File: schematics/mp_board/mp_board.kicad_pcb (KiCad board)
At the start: 4 copper layers, 49 parts, among them J1 i2c_1, J10 swd, J11 stm_boot, J17 rst_mcu, J2 i2c_2, J3 pins_b, J4 power_a, J6 MY_USB_B, J7 power_b, J8 pins_a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

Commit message: Placing components...
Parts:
- moved C5 104.2 mm to (169.5, 92.0), turned to -90 degrees
- moved C1 101.2 mm to (162.7, 92.2), turned to 90 degrees
- moved C28 100.6 mm to (151.7, 113.5), turned to 180 degrees
- moved J6 100.5 mm to (169.0, 102.8)
- moved J17 95.4 mm to (150.0, 35.0)
- moved R4 95.1 mm to (162.8, 103.8)
- moved C24 94.9 mm to (153.0, 111.8)
- moved C29 93.0 mm to (155.2, 98.5), turned to 90 degrees
- moved R3 92.0 mm to (158.7, 102.8), turned to 180 degrees
- moved C31 89.1 mm to (143.0, 113.5), turned to -90 degrees
- moved C27 87.7 mm to (153.5, 97.5), turned to 90 degrees
- moved C23 79.4 mm to (136.2, 106.5), turned to 180 degrees
- moved C30 78.0 mm to (140.0, 97.0), turned to 180 degrees
- moved U10 73.7 mm to (146.3, 104.2)
- moved J11 73.4 mm to (128.5, 50.0)
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
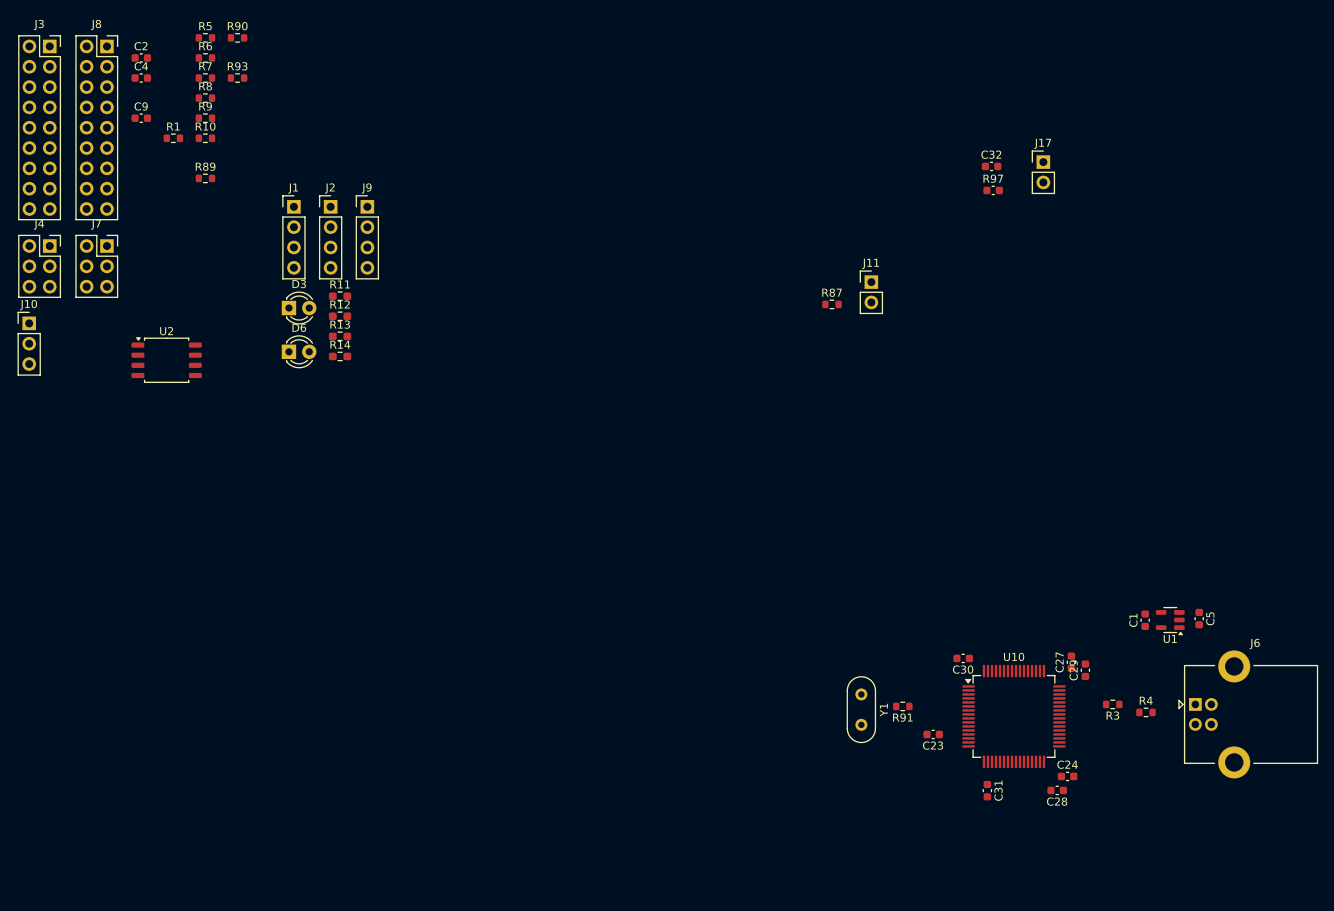
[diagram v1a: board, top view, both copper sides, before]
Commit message: Made tripple sockets. Mid pins are all ground for shielding.
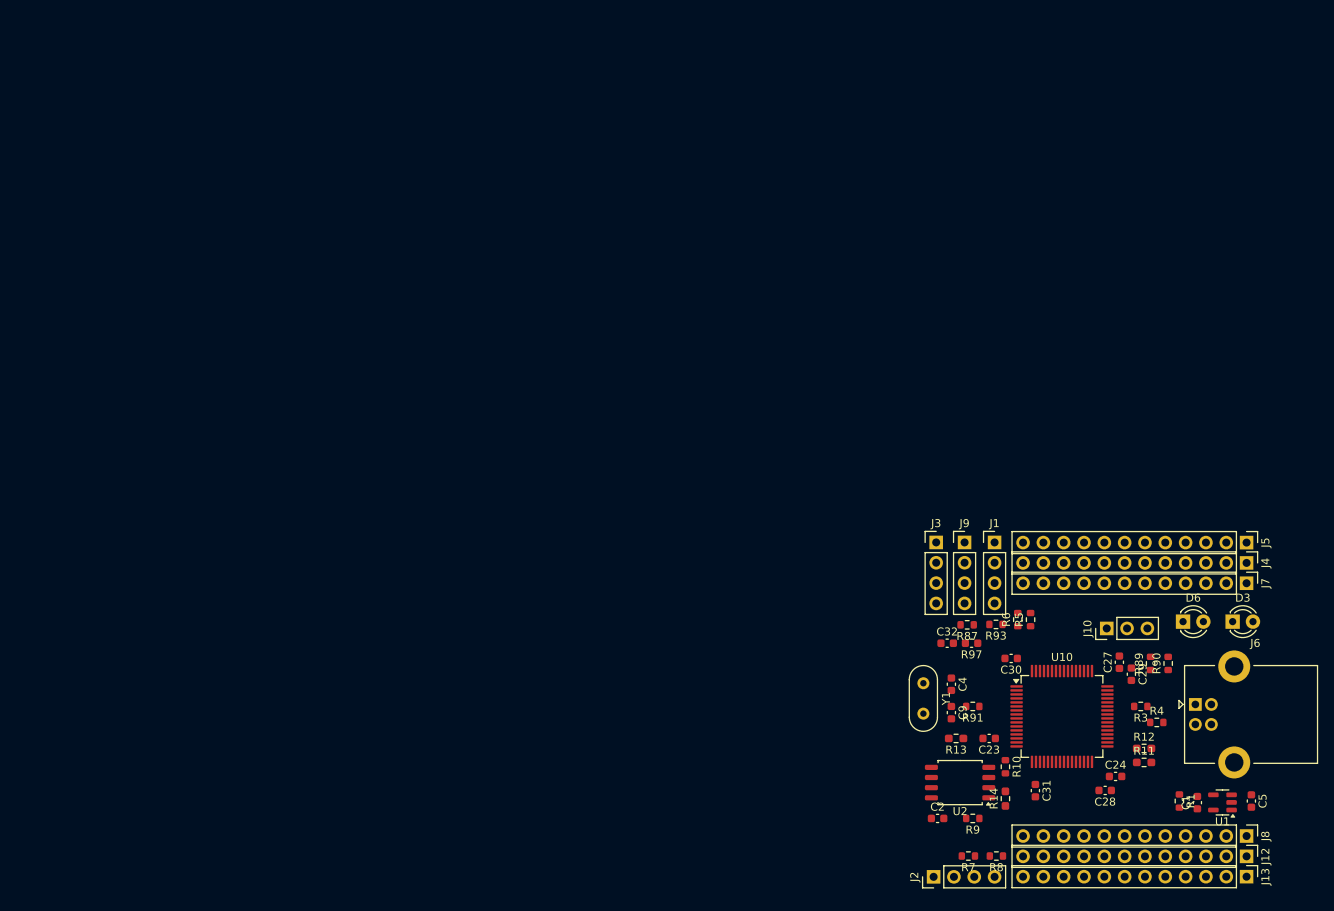
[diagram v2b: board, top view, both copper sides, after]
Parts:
- removed J11: stm_boot, Connector_PinHeader_2.54mm:PinHeader_1x02_P2.54mm_Vertical
- removed J17: rst_mcu, Connector_PinHeader_2.54mm:PinHeader_1x02_P2.54mm_Vertical
- added J12: pins_e, Connector_PinHeader_2.54mm:PinHeader_1x12_P2.54mm_Vertical, F.Cu at (175.4, 121.7)
- added J13: pins_f, Connector_PinHeader_2.54mm:PinHeader_1x12_P2.54mm_Vertical, F.Cu at (175.4, 124.3)
- added J5: pins_a, Connector_PinHeader_2.54mm:PinHeader_1x12_P2.54mm_Vertical, F.Cu at (175.4, 82.5)
- J3: value pins_b -> boot_rst; footprint Connector_PinSocket_2.54mm:PinSocket_2x09_P2.54mm_Vertical -> Connector_PinHeader_2.54mm:PinHeader_1x04_P2.54mm_Vertical
- J4: value power_a -> pins_b; footprint Connector_PinSocket_2.54mm:PinSocket_2x03_P2.54mm_Vertical -> Connector_PinHeader_2.54mm:PinHeader_1x12_P2.54mm_Vertical
- J7: value power_b -> pins_c; footprint Connector_PinSocket_2.54mm:PinSocket_2x03_P2.54mm_Vertical -> Connector_PinHeader_2.54mm:PinHeader_1x12_P2.54mm_Vertical
- J8: value pins_a -> pins_d; footprint Connector_PinSocket_2.54mm:PinSocket_2x09_P2.54mm_Vertical -> Connector_PinHeader_2.54mm:PinHeader_1x12_P2.54mm_Vertical
- moved J8 173.3 mm to (175.4, 119.2), turned to -90 degrees
- moved J4 154.8 mm to (175.4, 85.1), turned to -90 degrees
- moved R1 150.6 mm to (167.0, 114.8), turned to -90 degrees
- moved J7 148.6 mm to (175.4, 87.6), turned to -90 degrees
- moved R90 140.2 mm to (165.6, 97.6), turned to 90 degrees
- moved J10 140.0 mm to (157.9, 93.2), turned to 90 degrees
- moved C2 137.6 mm to (136.8, 117.0)
- moved R8 136.9 mm to (144.1, 121.7), turned to 180 degrees
- moved R7 136.2 mm to (140.6, 121.7), turned to 180 degrees
- moved R89 132.8 mm to (163.4, 97.6), turned to 90 degrees
- moved R9 129.9 mm to (141.2, 117.0), turned to 180 degrees
- moved R10 127.2 mm to (145.3, 110.5), turned to -90 degrees
- moved J3 127.0 mm to (136.6, 82.5)
- moved C4 126.5 mm to (138.5, 100.2), turned to -90 degrees
- moved R5 126.2 mm to (148.4, 92.2), turned to 90 degrees
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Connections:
- J3 pad 1: /pb14 -> /rst_mcu
- J3 pad 2: /pb15 -> GND
- J3 pad 3: /led-0 -> /boot0
- J3 pad 4: /pc0 -> VDD
- J4 pad 1: VDD -> GND
- J4 pad 3: /Vbus -> GND
- J4 pad 4: /Vbus -> GND
- J4 pad 6: VDD -> GND
- J7 pad 1: VDD -> /Vbus
- J7 pad 3: /Vbus -> VDD
- J7 pad 4: /Vbus -> /pa8
- J7 pad 5: GND -> /pb0
- J7 pad 6: VDD -> /pb1
- J8 pad 1: /pa0 -> /Vbus
- J8 pad 10: GND -> /pc5
- J8 pad 11: /pb8 -> /pc6
- J8 pad 12: /pb9 -> /pc15
- J8 pad 2: /pa1 -> GND
- J8 pad 3: /pa2 -> VDD
- J8 pad 4: /pa3 -> /pb14
- J8 pad 5: /pa4 -> /pb15
- J8 pad 6: /pa5 -> /led-0
- J8 pad 7: /pa6 -> /pc0
- J8 pad 8: /pa7 -> /pc1
- J8 pad 9: /pc14 -> /pc4

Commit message: a
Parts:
- moved R1 4.63 mm to (162.4, 114.3)
- moved R11 2.28 mm to (160.3, 110.1)
- moved R4 2.02 mm to (164.4, 103.0), turned to 180 degrees
- moved R3 1.98 mm to (163.5, 101.5)
- moved R12 0.79 mm to (161.8, 108.4)
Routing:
- net GND: track 0.00 -> 266.4 mm, vias 0 -> 21
- net /Vbus: track 0.00 -> 81.6 mm, vias 0 -> 4
- net VDD: track 0.00 -> 44.8 mm, vias 0 -> 7
- net /uart1-rx: track 0.00 -> 30.6 mm, vias 0 -> 2
- net /uart1-tx: track 0.00 -> 26.4 mm, vias 0 -> 1
- net /boot0: track 0.00 -> 21.4 mm
- net /spi2_miso: track 0.00 -> 21.1 mm
- net /rst_mcu: track 0.00 -> 13.8 mm
- net /boot1: track 0.00 -> 12.8 mm
- net /clk-in: track 0.00 -> 12.6 mm
- net /swd_io: track 0.00 -> 11.8 mm
- net /i2c1_sck: track 0.00 -> 10.7 mm
- net Net-(D3-K): track 0.00 -> 9.88 mm
- net Net-(J6-D+): track 0.00 -> 8.25 mm
- net /spi2_mosi: track 0.00 -> 7.27 mm
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
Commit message: Placing footprints, wiring.
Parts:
- moved C5 0.61 mm to (175.5, 115.2), turned to 90 degrees
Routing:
- net /i2c2_sck: track 0.00 -> 31.1 mm, vias 0 -> 2
- net /i2c2_sda: track 0.00 -> 28.1 mm, vias 0 -> 2
- net /rst_mcu: track 13.8 -> 33.8 mm, vias 0 -> 2
- net VDD: track 44.8 -> 49.5 mm, vias 7 -> 12
- net GND: track 266.4 -> 262.2 mm
- net /Vbus: track 81.6 -> 79.0 mm

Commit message: Wiring.
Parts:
- moved C5 0.27 mm to (175.5, 114.9), turned to -90 degrees
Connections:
- J13 pad 10: /pc13 -> /pa5
- J13 pad 11: /pd2 -> /pa3
- J13 pad 4: /pc7 -> /pb15
- J13 pad 5: /pc8 -> /pb0
- J13 pad 6: /pc9 -> /pa1
- J13 pad 8: /pc11 -> /pa2
- J13 pad 9: /pc12 -> /pa4
- J5 pad 10: /pa6 -> /pc13
- J5 pad 11: /pa7 -> /pc15
- J5 pad 12: /pc14 -> /pc0
- J5 pad 4: /pa0 -> /pc7
- J5 pad 5: /pa1 -> /pc9
- J5 pad 6: /pa2 -> /pc11
- J5 pad 7: /pa3 -> /pd2
- J5 pad 8: /pa4 -> /pb4
- J5 pad 9: /pa5 -> /pb8
- J7 pad 11: /pb8 -> /pc14
- J7 pad 4: /pa8 -> /pc6
- J7 pad 5: /pb0 -> /pc8
- J7 pad 6: /pb1 -> /pa8
- J7 pad 7: /pb3 -> /pc12
- J7 pad 8: /pb4 -> /pb3
- J8 pad 11: /pc6 -> /pb1
- J8 pad 12: /pc15 -> /pa6
- J8 pad 5: /pb15 -> /pa0
- J8 pad 7: /pc0 -> /pa7
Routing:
- net VDD: track 49.5 -> 273.1 mm, vias 12 -> 16
- net /pc7: track 0.00 -> 32.7 mm, vias 0 -> 1
- net /pc9: track 0.00 -> 31.4 mm, vias 0 -> 1
- net /flash_sck: track 1.26 -> 32.5 mm, vias 1 -> 2
- net /pb15: track 0.00 -> 30.7 mm, vias 0 -> 1
- net /pc0: track 0.00 -> 27.6 mm, vias 0 -> 1
- net /flash_cs: track 1.21 -> 27.0 mm, vias 1 -> 2
- net /pc6: track 0.00 -> 25.7 mm, vias 0 -> 1
- net /pc15: track 0.00 -> 24.9 mm, vias 0 -> 1
- net /pa8: track 0.00 -> 24.5 mm, vias 0 -> 1
- net /pc13: track 0.00 -> 24.0 mm, vias 0 -> 1
- net /pb8: track 0.00 -> 22.2 mm, vias 0 -> 1
- net /pc8: track 0.00 -> 22.0 mm, vias 0 -> 1
- net /pc14: track 0.00 -> 21.2 mm, vias 0 -> 1
- net /pc11: track 0.00 -> 20.3 mm
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
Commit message: Wiring.
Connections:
- J13 pad 10: /pa5 -> /pa3
- J13 pad 11: /pa3 -> /pa1
- J13 pad 4: /pb15 -> /pc6
- J13 pad 5: /pb0 -> /pb14
- J13 pad 6: /pa1 -> /pb1
- J13 pad 7: /led-1 -> /pc5
- J13 pad 8: /pa2 -> /pa7
- J13 pad 9: /pa4 -> /pa5
- J5 pad 4: /pc7 -> /pc9
- J5 pad 5: /pc9 -> /led-0
- J7 pad 4: /pc6 -> /pc8
- J7 pad 5: /pc8 -> /pa8
- J7 pad 6: /pa8 -> /led-1
- J8 pad 10: /pc5 -> /pa2
- J8 pad 11: /pb1 -> /pa0
- J8 pad 12: /pa6 -> /pc1
- J8 pad 4: /pb14 -> /pc7
- J8 pad 5: /pa0 -> /pb15
- J8 pad 6: /led-0 -> /pb0
- J8 pad 7: /pa7 -> /pc4
- J8 pad 8: /pc1 -> /pa6
- J8 pad 9: /pc4 -> /pa4
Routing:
- net VDD: track 273.1 -> 313.8 mm, vias 16 -> 19
- net /pc1: track 0.00 -> 30.5 mm, vias 0 -> 1
- net /led-0: track 10.6 -> 35.1 mm
- net /pa7: track 0.00 -> 22.9 mm, vias 0 -> 1
- net /pb1: track 0.00 -> 22.3 mm
- net /pc5: track 0.00 -> 21.2 mm
- net /pa3: track 0.00 -> 20.4 mm
- net /pa1: track 0.00 -> 20.2 mm, vias 0 -> 1
- net /pa5: track 0.00 -> 18.8 mm, vias 0 -> 1
- net /pb0: track 0.00 -> 16.1 mm
- net /pa0: track 0.00 -> 16.1 mm, vias 0 -> 1
- net /pa2: track 0.00 -> 16.0 mm
- net /pc4: track 0.00 -> 15.4 mm, vias 0 -> 1
- net /led-1: track 16.1 -> 29.8 mm
- net /pa6: track 0.00 -> 13.6 mm, vias 0 -> 1
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
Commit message: Wiring...
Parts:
- moved R87 0.78 mm to (139.7, 92.8)
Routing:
- net GND: track 273.5 -> 320.5 mm, vias 25 -> 43
- net VDD: track 313.8 -> 337.4 mm, vias 19 -> 25
- net /pc7: track 23.9 -> 21.3 mm
- net /uart1-tx: track 28.3 -> 30.5 mm, vias 1 -> 2
- net /flash_cs: track 29.5 -> 27.8 mm
- net /Vbus: track 83.5 -> 81.8 mm
- net /i2c2_sck: track 29.9 -> 28.6 mm
- net /pc0: track 27.1 -> 28.0 mm
- net /flash_sck: track 31.0 -> 30.4 mm
- net /pa0: track 16.1 -> 15.6 mm
- added copper zone on B.Cu, net GND
- added copper zone on F.Cu, net GND
- added copper zone on In1.Cu, net GND
- added copper zone on In2.Cu, net GND
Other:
- board outline added: 45.5 x 46 mm

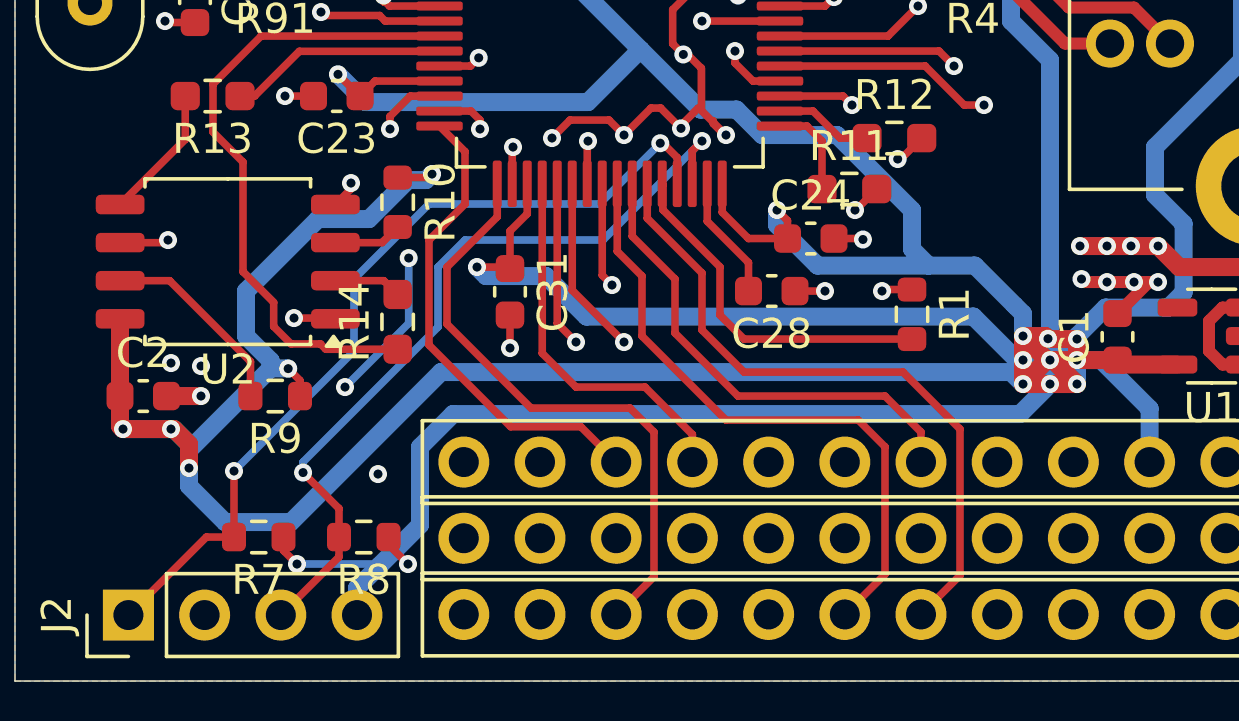
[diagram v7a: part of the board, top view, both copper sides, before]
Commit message: Slightly moved a Vdd line going to the flash chip.
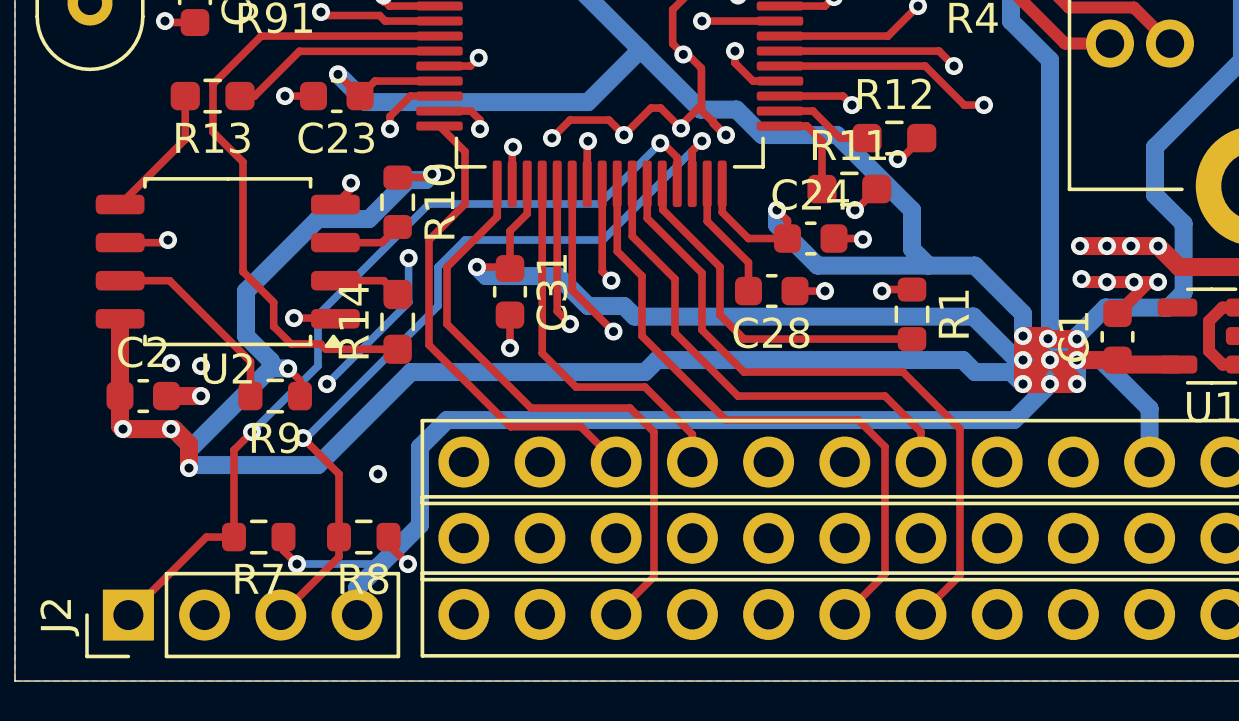
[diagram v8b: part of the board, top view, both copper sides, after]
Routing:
- net VDD: track 337.4 -> 335.2 mm
